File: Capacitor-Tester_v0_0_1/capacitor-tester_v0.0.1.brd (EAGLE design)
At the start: 100 x 80 mm, 30 parts, among them IC1 AD8531ARZ, IC2 MC34063EBD-TR, J1 USB4125-GF-A-0190_REVA2, J2 DS1044-140G, J4 250-103, U1 AD5933, U2 LM6171AIMX/NOPB, Y1 LFSPXO018034

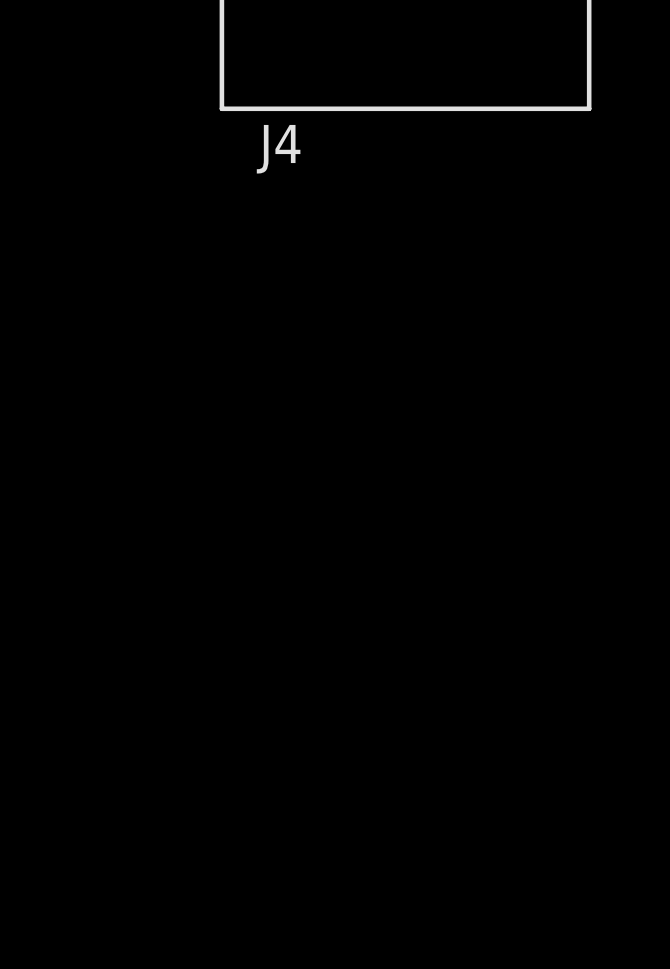
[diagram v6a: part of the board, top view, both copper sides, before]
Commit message: v0.0.1 - Version control. Added DAC6571
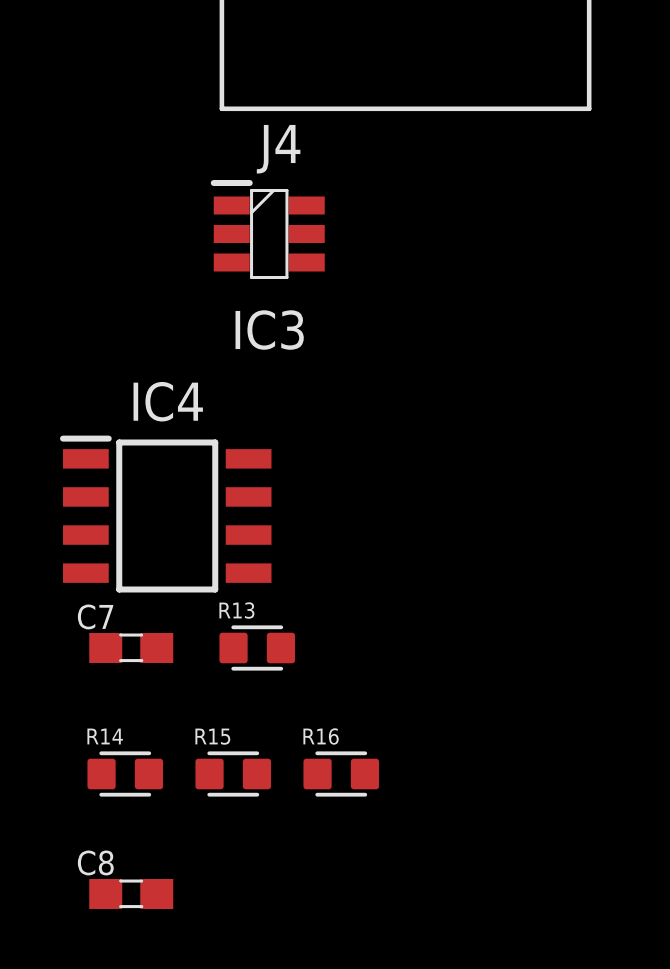
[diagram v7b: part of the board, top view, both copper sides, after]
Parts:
- added C7: 1u, custom_library:C0603
- added C8: 10u, custom_library:C0603
- added IC3: DAC6571IDBVT, DAC6571IDBVT:SOT95P280X145-6N
- added IC4: AD8531ARZ, AD8531ARZ:SOIC127P600X175-8N
- added R13, R15, R16: 20k-1%, custom_library:R0603
- added R14: 4k-1%, custom_library:R0603
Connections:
- new net DAC_OUT: IC3.1
- new net N$12: C7.1, IC4.3, R15.2, R16.1
- new net N$9: IC4.2, R13.1, R14.1
- net +5V: now also C8.1, IC3.3, IC4.7, R15.1
- net GND: now also C7.2, C8.2, IC3.2, IC3.6, IC4.4, R16.2
- net OPAMP_OUT: now also IC4.6, R14.2
- net SCL: now also IC3.5
- net SDA: now also IC3.4
- net VOUT: now also R13.2
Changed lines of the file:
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@@
 <attribute name="NAME" x="-104.5334" y="-213.435" size="1.27" layer="25" ratio="6" rot="SR0"/>
+</element>
+<element name="IC3" library="DAC6571IDBVT" package="SOT95P280X145-6N" value="DAC6571IDBVT" x="-104.2" y="-215.8" smashed="yes">
+<attribute name="DESCRIPTION" value="Texas Instruments DAC6571IDBVT, 10 bit Serial DAC, 188ksps, 6-Pin SOT-23" x="-104.2" y="-215.8" size="1.778" layer="27" display="off"/>
+<attribute name="HEIGHT" value="1.45mm" x="-104.2" y="-215.8" size="1.778" layer="27" display="off"/>
+<attribute name="MANUFACTURER_NAME" value="Texas Instruments" x="-104.2" y="-215.8" size="1.778" layer="27" display="off"/>
+<attribute name="MANUFACTURER_PART_NUMBER" value="DAC6571IDBVT" x="-104.2" y="-215.8" size="1.778" layer="27" display="off"/>
+<attribute name="MOUSER_PART_NUMBER" value="595-DAC6571IDBVT" x="-104.2" y="-215.8" size="1.778" layer="27" display="off"/>
+<attribute name="MOUSER_PRICE-STOCK" value="https://www.mouser.co.uk/ProductDetail/Texas-Instruments/DAC6571IDBVT?qs=vul0MlC%2Fa1dqpnhoFf%252B88g%3D%3D" x="-104.2" y="-215.8" size="1.778" layer="27" display="off"/>
+<attribute name="NAME" x="-104.2" y="-219" size="1.27" layer="25" align="center"/>
+<attribute name="VALUE" x="-104.2" y="-215.8" size="1.27" layer="27" align="center"/>
+</element>
+<element name="IC4" library="AD8531ARZ" package="SOIC127P600X175-8N" value="AD8531ARZ" x="-107.6" y="-225.2" smashed="yes">
+<attribute name="DESCRIPTION" value="250 mA Output, Low Cost, Single-Supply Amplifier" x="-115" y="-217.4" size="1.778" layer="27" display="off"/>
+<attribute name="HEIGHT" value="1.75mm" x="-115" y="-217.4" size="1.778" layer="27" display="off"/>
+<attribute name="MANUFACTURER_NAME" value="Analog Devices" x="-115" y="-217.4" size="1.778" layer="27" display="off"/>
+<attribute name="MANUFACTURER_PART_NUMBER" value="AD8531ARZ" x="-115" y="-217.4" size="1.778" layer="27" display="off"/>
+<attribute name="MOUSER_PART_NUMBER" value="584-AD8531ARZ" x="-115" y="-217.4" size="1.778" layer="27" display="off"/>
+<attribute name="MOUSER_PRICE-STOCK" value="https://www.mouser.co.uk/ProductDetail/Analog-Devices/AD8531ARZ?qs=%2FtpEQrCGXCxqCqynf0JWOw%3D%3D" x="-115" y="-217.4" size="1.778" layer="27" display="off"/>
+<attribute name="NAME" x="-107.6" y="-221.39" size="1.27" layer="25" align="center"/>
+</element>
+<element name="R13" library="custom_library" package="R0603" value="20k-1%" x="-104.6" y="-229.6" smashed="yes">
+<attribute name="NAME" x="-105.92476875" y="-228.613721875" size="0.52744375" layer="25"/>
+<attribute name="VALUE" x="-106.319259375" y="-231.12958125" size="0.525771875" layer="27"/>
+</element>
+<element name="R14" library="custom_library" package="R0603" value="4k-1%" x="-109" y="-233.8" smashed="yes">
+<attribute name="NAME" x="-110.32476875" y="-232.813721875" size="0.52744375" layer="25"/>
+<attribute name="VALUE" x="-110.719259375" y="-235.32958125" size="0.525771875" layer="27"/>
+</element>
+<element name="C7" library="custom_library" package="C0603" value="1u" x="-108.8" y="-229.6" smashed="yes">
+<attribute name="NAME" x="-110.635" y="-228.965" size="0.8" layer="25"/>
+<attribute name="VALUE" x="-109.435" y="-231.505" size="1.27" layer="27"/>
+</element>
+<element name="R15" library="custom_library" package="R0603" value="20k-1%" x="-105.4" y="-233.8" smashed="yes">
+<attribute name="NAME" x="-106.72476875" y="-232.813721875" size="0.52744375" layer="25"/>
+<attribute name="VALUE" x="-107.119259375" y="-235.32958125" size="0.525771875" layer="27"/>
+</element>
+<element name="R16" library="custom_library" package="R0603" value="20k-1%" x="-101.8" y="-233.8" smashed="yes">
+<attribute name="NAME" x="-103.12476875" y="-232.813721875" size="0.52744375" layer="25"/>
+<attribute name="VALUE" x="-103.519259375" y="-235.32958125" size="0.525771875" layer="27"/>
+</element>
+<element name="C8" library="custom_library" package="C0603" value="10u" x="-108.8" y="-237.8" smashed="yes">
+<attribute name="NAME" x="-110.635" y="-237.165" size="0.8" layer="25"/>
+<attribute name="VALUE" x="-109.435" y="-239.705" size="1.27" layer="27"/>
 </element>
 </elements>
@@
 <contactref element="C6" pad="2"/>
 <contactref element="R10" pad="2"/>
+<contactref element="IC3" pad="2"/>
+<contactref element="IC3" pad="6"/>
+<contactref element="IC4" pad="4"/>
+<contactref element="C7" pad="2"/>
+<contactref element="R16" pad="2"/>
+<contactref element="C8" pad="2"/>
 <wire x1="-44.61" y1="-181.6" x2="-51.5" y2="-188" width="0" layer="19" extent="1-1"/>
 <wire x1="-39.3" y1="-188" x2="-44.61" y2="-181.6" width="0" layer="19" extent="1-1"/>
@@
 <wire x1="-4.94" y1="-167.11" x2="-33.712" y2="-171.965" width="0" layer="19" extent="1-1"/>
 <wire x1="-4.94" y1="-165.84" x2="-4.94" y2="-167.11" width="0" layer="19" extent="1-1"/>
+<wire x1="-102.95" y1="-214.85" x2="-74.35" y2="-195.4" width="0" layer="19" extent="1-1"/>
+<wire x1="-105.45" y1="-215.8" x2="-102.95" y2="-214.85" width="0" layer="19" extent="1-1"/>
+<wire x1="-110.312" y1="-227.105" x2="-105.45" y2="-215.8" width="0" layer="19" extent="1-1"/>
+<wire x1="-107.95" y1="-229.6" x2="-110.312" y2="-227.105" width="0" layer="19" extent="1-1"/>
+<wire x1="-101.01" y1="-233.8" x2="-107.95" y2="-229.6" width="0" layer="19" extent="1-1"/>
+<wire x1="-107.95" y1="-237.8" x2="-101.01" y2="-233.8" width="0" layer="19" extent="1-1"/>
 <wire x1="-16.95" y1="-115.2" x2="-4.94" y2="-165.84" width="0" layer="19" extent="1-1"/>
 <wire x1="-24.41" y1="-115.4" x2="-16.95" y2="-115.2" width="0" layer="19" extent="1-1"/>
@@
 <contactref element="C5" pad="1"/>
 <contactref element="R11" pad="1"/>
+<contactref element="IC3" pad="3"/>
+<contactref element="IC4" pad="7"/>
+<contactref element="R15" pad="1"/>
+<contactref element="C8" pad="1"/>
 <wire x1="-56.5" y1="-188" x2="-61.19" y2="-189.2" width="0" layer="19" extent="1-1"/>
 <wire x1="-28.288" y1="-173.235" x2="-56.5" y2="-188" width="0" layer="19" extent="1-1"/>
+<wire x1="-105.45" y1="-216.75" x2="-61.19" y2="-189.2" width="0" layer="19" extent="1-1"/>
+<wire x1="-104.888" y1="-224.565" x2="-105.45" y2="-216.75" width="0" layer="19" extent="1-1"/>
+<wire x1="-106.19" y1="-233.8" x2="-104.888" y2="-224.565" width="0" layer="19" extent="1-1"/>
+<wire x1="-109.65" y1="-237.8" x2="-106.19" y2="-233.8" width="0" layer="19" extent="1-1"/>
 <wire x1="-22.59" y1="-115.4" x2="-28.288" y2="-173.235" width="0" layer="19" extent="1-1"/>
 <wire x1="0" y1="-107.675" x2="-22.59" y2="-115.4" width="0" layer="19" extent="1-1"/>
@@
 <contactref element="R1" pad="1"/>
 <contactref element="J4" pad="2"/>
+<contactref element="IC3" pad="5"/>
 <wire x1="0" y1="-12.7" x2="-11.99" y2="-86.8" width="0" layer="19" extent="1-1"/>
 <wire x1="-98.8948" y1="-206.8" x2="-11.99" y2="-86.8" width="0" layer="19" extent="1-1"/>
+<wire x1="-102.95" y1="-215.8" x2="-98.8948" y2="-206.8" width="0" layer="19" extent="1-1"/>
 </signal>
 <signal name="SDA">
@@
 <contactref element="R3" pad="1"/>
 <contactref element="J4" pad="1"/>
+<contactref element="IC3" pad="4"/>
 <wire x1="0" y1="-13.35" x2="-7.99" y2="-86.8" width="0" layer="19" extent="1-1"/>
 <wire x1="-102.4" y1="-206.8" x2="-7.99" y2="-86.8" width="0" layer="19" extent="1-1"/>
+<wire x1="-102.95" y1="-216.75" x2="-102.4" y2="-206.8" width="0" layer="19" extent="1-1"/>
 </signal>
 <signal name="MCLK">
@@
 <contactref element="U1" pad="6"/>
 <contactref element="R2" pad="2"/>
+<contactref element="R13" pad="2"/>
 <wire x1="-7.01" y1="-15.95" x2="-14.21" y2="-111.2" width="0" layer="19" extent="1-1"/>
+<wire x1="-103.81" y1="-229.6" x2="-14.21" y2="-111.2" width="0" layer="19" extent="1-1"/>
 </signal>
 <signal name="N$1">
@@
 <contactref element="J2" pad="3"/>
 <contactref element="J2" pad="2"/>
+<contactref element="IC4" pad="6"/>
+<contactref element="R14" pad="2"/>
 <wire x1="-7.62" y1="-140.8" x2="-7.62" y2="-143.34" width="0" layer="19" extent="1-1"/>
 <wire x1="-7.62" y1="-138.26" x2="-7.62" y2="-140.8" width="0" layer="19" extent="1-1"/>
@@
 <wire x1="-17.61" y1="-111.2" x2="-7.62" y2="-128.1" width="0" layer="19" extent="1-1"/>
 <wire x1="0" y1="-108.945" x2="-17.61" y2="-111.2" width="0" layer="19" extent="1-1"/>
+<wire x1="-104.888" y1="-225.835" x2="-7.62" y2="-143.34" width="0" layer="19" extent="1-1"/>
+<wire x1="-108.21" y1="-233.8" x2="-104.888" y2="-225.835" width="0" layer="19" extent="1-1"/>
 </signal>
 <signal name="N$4">
@@
 <wire x1="-7.01" y1="-17.25" x2="-5.53" y2="-68" width="0" layer="19" extent="1-1"/>
 </signal>
+<signal name="DAC_OUT">
+<contactref element="IC3" pad="1"/>
+</signal>
+<signal name="N$9">
+<contactref element="R13" pad="1"/>
+<contactref element="IC4" pad="2"/>
+<contactref element="R14" pad="1"/>
+<wire x1="-105.39" y1="-229.6" x2="-109.79" y2="-233.8" width="0" layer="19" extent="1-1"/>
+<wire x1="-110.312" y1="-224.565" x2="-105.39" y2="-229.6" width="0" layer="19" extent="1-1"/>
+</signal>
+<signal name="N$12">
+<contactref element="IC4" pad="3"/>
+<contactref element="C7" pad="1"/>
+<contactref element="R15" pad="2"/>
+<contactref element="R16" pad="1"/>
+<wire x1="-110.312" y1="-225.835" x2="-109.65" y2="-229.6" width="0" layer="19" extent="1-1"/>
+<wire x1="-104.61" y1="-233.8" x2="-109.65" y2="-229.6" width="0" layer="19" extent="1-1"/>
+<wire x1="-102.59" y1="-233.8" x2="-104.61" y2="-233.8" width="0" layer="19" extent="1-1"/>
+</signal>
 </signals>
